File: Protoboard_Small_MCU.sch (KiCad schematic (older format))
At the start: 55 parts, among them J1 POWER, P1 CONN_6, P10 3pin, P11 3pin, P12 3pin, P13 3pin, P14 3pin, P15 3pin, P16 3pin, P17 3pin, P18 2pin, P19 2pin, P2 CONN_6, P20 1pin, P21 2pin, P22 3pin, P23 3pin, P24 3pin, P25 3pin, P26 3pin, P27 3pin, P28 3pin, P29 3pin, P3 1pin, P30 3pin, P31 3pin, P32 3pin, P33 3pin, P34 3pin, P35 3pin, P36 2pin, P37 CONN_7, P38 CONN_7, P39 CONN_7, P4 3pin, P40 CONN_7, P41 V+_RAIL, P42 V-_RAIL, P43 V+_RAIL, P44 V-_RAIL, P45 CONN_8, P46 CONN_8, P47 CONN_8, P48 CONN_8, P49 1pin, P5 3pin, P50 1pin, P51 CONN_6, P52 CONN_6, P6 3pin, P7 3pin, P8 3pin, P9 3pin, SW1 PUSH_SWITCH, U1 DIP28

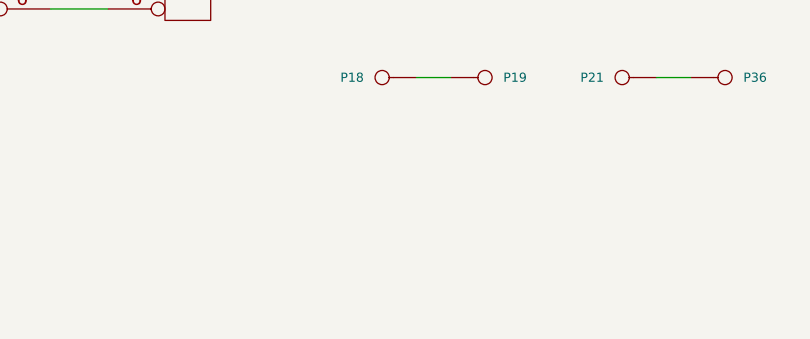
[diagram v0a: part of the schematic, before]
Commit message: Add mounting holes. Greatly increase trace widths. Modify silkscreen to make room for changes.
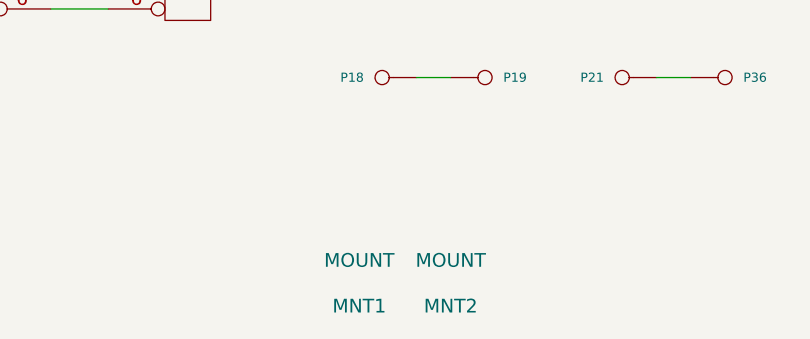
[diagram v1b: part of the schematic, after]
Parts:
- added MNT1, MNT2: MOUNT, symbol MOUNT
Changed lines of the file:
@@
-EESchema Schematic File Version 2  date 1/26/2012 6:15:53 AM
-LIBS:z_audio
-LIBS:z_clock
-LIBS:z_connector
-LIBS:z_digital
-LIBS:z_discrete
-LIBS:z_microcontroller
-LIBS:z_power
-LIBS:z_transducer
-LIBS:z_vintage_ic
+EESchema Schematic File Version 2  date 2/14/2012 2:29:37 AM
+LIBS:zach_components
 LIBS:power
 LIBS:device
@@
 Sheet 1 1
 Title "Protoboard for up to 18pin Microcontrollers (AVR & PIC)"
-Date "26 jan 2012"
+Date "14 feb 2012"
 Rev "1"
 Comp "Zachary Heilig"
@@
 $EndDescr
 $Comp
+L MOUNT MNT2
+U 1 1 4F3A17D5
+P 3800 3650
+F 0 "MNT2" H 3800 3550 60  0000 C CNN
+F 1 "MOUNT" H 3800 3750 60  0000 C CNN
+	1    3800 3650
+	1    0    0    -1
+$EndComp
+$Comp
+L MOUNT MNT1
+U 1 1 4F3A17D3
+P 3400 3650
+F 0 "MNT1" H 3400 3550 60  0000 C CNN
+F 1 "MOUNT" H 3400 3750 60  0000 C CNN
+	1    3400 3650
+	1    0    0    -1
+$EndComp
+$Comp
 L CONN_6 P52

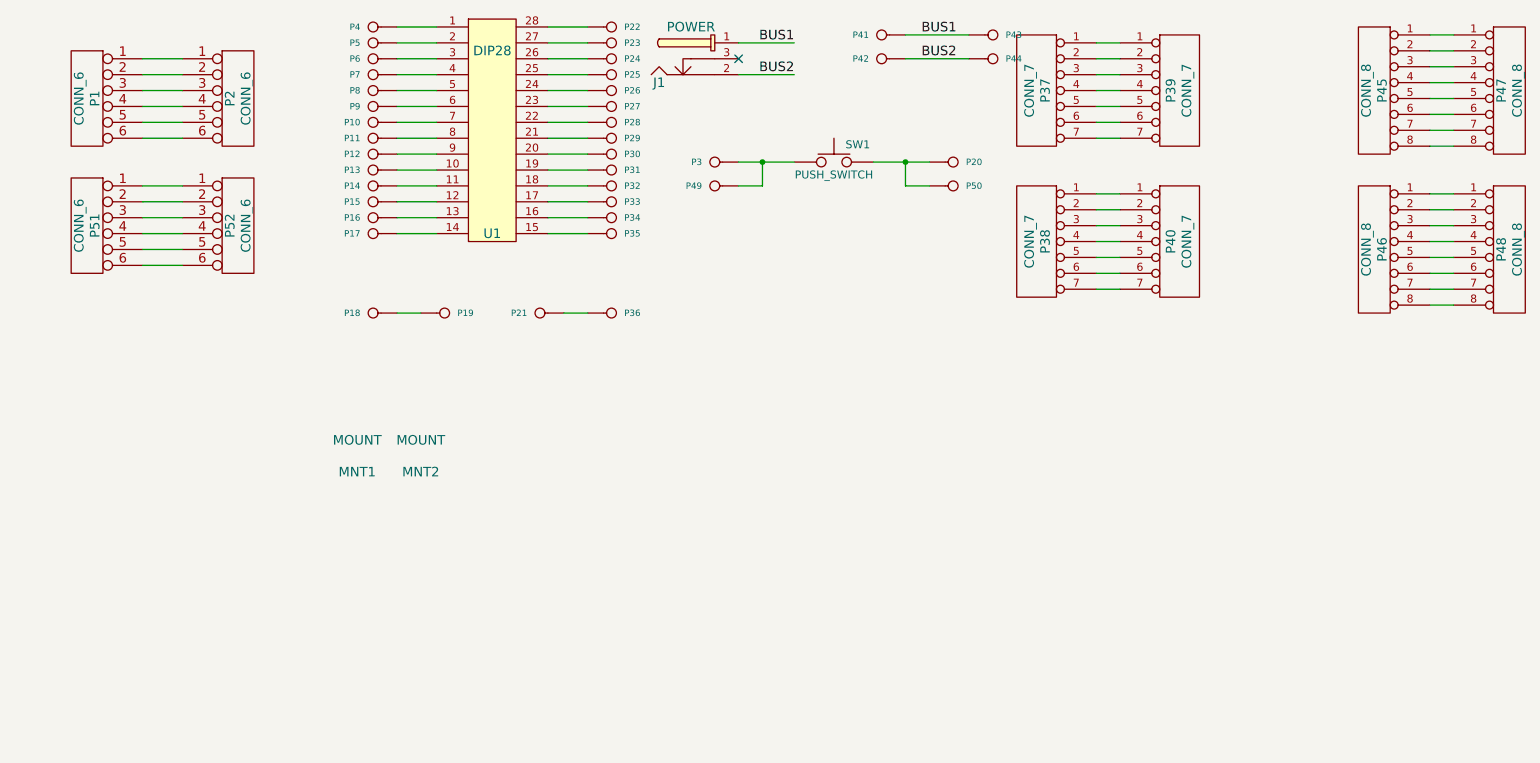
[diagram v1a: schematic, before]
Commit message: Added LDO option to power section.
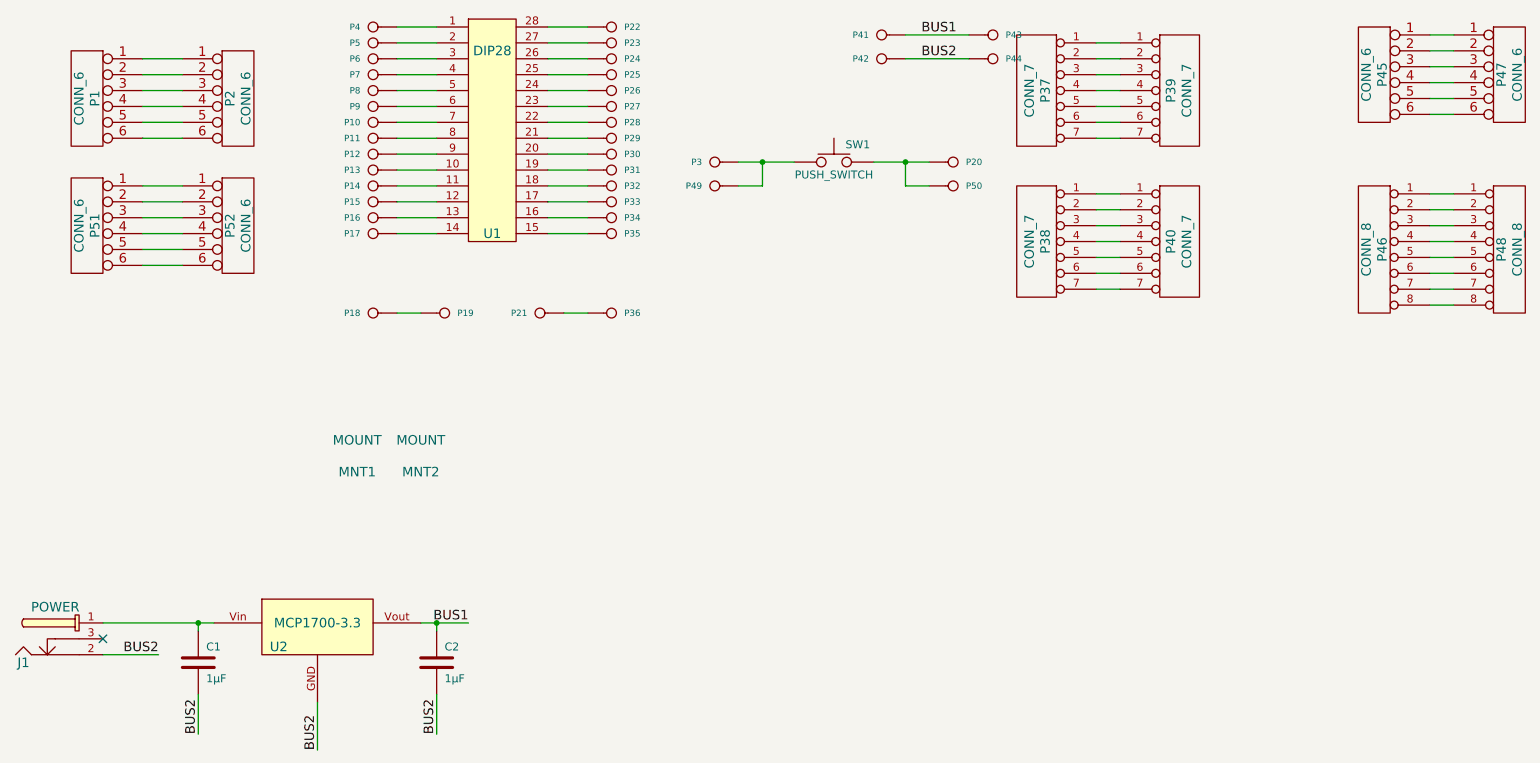
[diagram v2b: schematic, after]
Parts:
- removed P45, P47: CONN_8, symbol CONN_8
- added C1, C2: 1µF, SMD1608-NP, symbol C
- added P45, P47: CONN_6, symbol CONN_6
- added U2: MCP1700-3.3, MCP1700-TO92, symbol MCP1700-3.3
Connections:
- net BUS1: now also C2.1, U2.Vout; no longer J1.1
- net BUS2: now also C1.2, C2.2, U2.GND
- new net: C1.1, J1.1, U2.Vin
- new net: P45.1, P47.1
- new net: P45.2, P47.2
- new net: P45.3, P47.3
- new net: P45.4, P47.4
- new net: P45.5, P47.5
- new net: P45.6, P47.6
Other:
- moved on the sheet: J1
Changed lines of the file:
@@
-EESchema Schematic File Version 2  date 2/14/2012 2:29:37 AM
+EESchema Schematic File Version 2  date 3/18/2012 2:29:13 AM
 LIBS:zach_components
 LIBS:power
@@
 Sheet 1 1
 Title "Protoboard for up to 18pin Microcontrollers (AVR & PIC)"
-Date "14 feb 2012"
+Date "18 mar 2012"
 Rev "1"
 Comp "Zachary Heilig"
@@
 $EndDescr
 $Comp
+L CONN_6 P47
+U 1 1 4F6584D9
+P 10650 1250
+F 0 "P47" V 10600 1250 60  0000 C CNN
+F 1 "CONN_6" V 10700 1250 60  0000 C CNN
+	1    10650 1250
+	1    0    0    -1
+$EndComp
+$Comp
+L CONN_6 P45
+U 1 1 4F6584CB
+P 9800 1250
+F 0 "P45" V 9750 1250 60  0000 C CNN
+F 1 "CONN_6" V 9850 1250 60  0000 C CNN
+	1    9800 1250
+	-1   0    0    -1
+$EndComp
+Wire Wire Line
+	3900 5150 3900 5400
+Connection ~ 2400 4700
+Wire Wire Line
+	2400 4750 2400 4700
+Wire Wire Line
+	3150 5200 3150 5500
+Wire Wire Line
+	2500 4700 1800 4700
+Connection ~ 6850 1800
+Wire Wire Line
+	6850 1800 6850 1950
+Wire Wire Line
+	6850 1950 7000 1950
+Wire Wire Line
+	1800 4900 2150 4900
+Wire Wire Line
+	10150 2700 10300 2700
+Wire Wire Line
+	10150 2600 10300 2600
+Wire Wire Line
+	10150 2400 10300 2400
+Wire Wire Line
+	10150 2200 10300 2200
+Wire Wire Line
+	10150 2000 10300 2000
+Wire Wire Line
+	10150 2100 10300 2100
+Wire Wire Line
+	10150 2300 10300 2300
+Wire Wire Line
+	10150 2500 10300 2500
+Wire Wire Line
+	10150 1500 10300 1500
+Wire Wire Line
+	10150 1300 10300 1300
+Wire Wire Line
+	10150 1100 10300 1100
+Wire Wire Line
+	10150 1000 10300 1000
+Wire Wire Line
+	10150 1200 10300 1200
+Wire Wire Line
+	10150 1400 10300 1400
+Wire Wire Line
+	8050 2500 8200 2500
+Wire Wire Line
+	8050 2300 8200 2300
+Wire Wire Line
+	8050 2100 8200 2100
+Wire Wire Line
+	8050 2000 8200 2000
+Wire Wire Line
+	8050 2200 8200 2200
+Wire Wire Line
+	8050 2400 8200 2400
+Wire Wire Line
+	8050 2600 8200 2600
+Wire Wire Line
+	8050 1650 8200 1650
+Wire Wire Line
+	8050 1450 8200 1450
+Wire Wire Line
+	8050 1250 8200 1250
+Wire Wire Line
+	8050 1050 8200 1050
+Wire Wire Line
+	7250 1000 6850 1000
+Wire Wire Line
+	3650 2750 3800 2750
+Wire Wire Line
+	3650 2250 3900 2250
+Wire Wire Line
+	3650 2050 3900 2050
+Wire Wire Line
+	3650 1950 3900 1950
+Wire Wire Line
+	3650 2150 3900 2150
+Wire Wire Line
+	4600 2150 4850 2150
+Wire Wire Line
+	4600 1950 4850 1950
+Wire Wire Line
+	4600 2050 4850 2050
+Wire Wire Line
+	4600 2250 4850 2250
+Wire Wire Line
+	2050 1650 2300 1650
+Wire Wire Line
+	2050 1450 2300 1450
+Wire Wire Line
+	2050 1250 2300 1250
+Wire Wire Line
+	2050 1150 2300 1150
+Wire Wire Line
+	2050 1350 2300 1350
+Wire Wire Line
+	2050 1550 2300 1550
+Wire Wire Line
+	3650 1750 3900 1750
+Wire Wire Line
+	3650 1550 3900 1550
+Wire Wire Line
+	3650 1350 3900 1350
+Wire Wire Line
+	3650 1150 3900 1150
+Wire Wire Line
+	3650 950  3900 950
+Wire Wire Line
+	3650 1050 3900 1050
+Wire Wire Line
+	3650 1250 3900 1250
+Wire Wire Line
+	3650 1450 3900 1450
+Wire Wire Line
+	3650 1650 3900 1650
+Wire Wire Line
+	3650 1850 3900 1850
+Wire Wire Line
+	4600 1850 4850 1850
+Wire Wire Line
+	4600 1650 4850 1650
+Wire Wire Line
+	4600 1450 4850 1450
+Wire Wire Line
+	4600 1250 4850 1250
+Wire Wire Line
+	4600 1050 4850 1050
+Wire Wire Line
+	4600 950  4850 950
+Wire Wire Line
+	4600 1150 4850 1150
+Wire Wire Line
+	4600 1350 4850 1350
+Wire Wire Line
+	4600 1550 4850 1550
+Wire Wire Line
+	4600 1750 4850 1750
+Wire Wire Line
+	6150 1800 5800 1800
+Wire Wire Line
+	7000 1800 6650 1800
+Wire Wire Line
+	4700 2750 4850 2750
+Wire Wire Line
+	6850 1150 7250 1150
+Wire Wire Line
+	8050 1150 8200 1150
+Wire Wire Line
+	8050 1350 8200 1350
+Wire Wire Line
+	8050 1550 8200 1550
+Wire Wire Line
+	5800 1950 5950 1950
+Wire Wire Line
+	5950 1950 5950 1800
+Connection ~ 5950 1800
+Wire Wire Line
+	2050 2350 2300 2350
+Wire Wire Line
+	2050 2150 2300 2150
+Wire Wire Line
+	2050 1950 2300 1950
+Wire Wire Line
+	2050 2050 2300 2050
+Wire Wire Line
+	2050 2250 2300 2250
+Wire Wire Line
+	2050 2450 2300 2450
+Wire Wire Line
+	3800 4700 4100 4700
+Wire Wire Line
+	3900 4750 3900 4700
+Connection ~ 3900 4700
+Wire Wire Line
+	2400 5150 2400 5400
+Text Label 3900 5400 1    60   ~ 0
+BUS2
+Text Label 2400 5400 1    60   ~ 0
+BUS2
+$Comp
+L C C1
+U 1 1 4F65842D
+P 2400 4950
+F 0 "C1" H 2450 5050 50  0000 L CNN
+F 1 "1µF" H 2450 4850 50  0000 L CNN
+F 2 "SMD1608-NP" H 2400 4950 60  0001 C CNN
+	1    2400 4950
+	1    0    0    -1
+$EndComp
+$Comp
+L C C2
+U 1 1 4F658426
+P 3900 4950
+F 0 "C2" H 3950 5050 50  0000 L CNN
+F 1 "1µF" H 3950 4850 50  0000 L CNN
+F 2 "SMD1608-NP" H 3900 4950 60  0001 C CNN
+	1    3900 4950
+	1    0    0    -1
+$EndComp
+Text Label 3150 5500 1    60   ~ 0
+BUS2
+$Comp
+L MCP1700-3.3 U2
+U 1 1 4F658410
+P 3150 4700
+F 0 "U2" H 2850 4550 60  0000 L CNN
+F 1 "MCP1700-3.3" H 3150 4700 60  0000 C CNN
+F 2 "MCP1700-TO92" H 3150 4800 60  0001 C CNN
+	1    3150 4700
+	1    0    0    -1
+$EndComp
+$Comp
 L MOUNT MNT2
 U 1 1 4F3A17D5
@@
 	-1   0    0    -1
 $EndComp
-Wire Wire Line
-	2050 2450 2300 2450
-Wire Wire Line
-	2050 2250 2300 2250
-Wire Wire Line
-	2050 2050 2300 2050
-Wire Wire Line
-	2050 1950 2300 1950
-Wire Wire Line
-	2050 2150 2300 2150
-Wire Wire Line
-	2050 2350 2300 2350
-Connection ~ 5950 1800
-Wire Wire Line
-	5950 1800 5950 1950
-Wire Wire Line
-	5950 1950 5800 1950
-Wire Wire Line
-	5800 1050 6150 1050
-Wire Wire Line
-	10300 1700 10150 1700
-Wire Wire Line
-	8050 1550 8200 1550
-Wire Wire Line
-	8050 1350 8200 1350
-Wire Wire Line
-	8050 1150 8200 1150
-Wire Wire Line
-	6850 1150 7250 1150
-Wire Wire Line
-	4700 2750 4850 2750
-Wire Wire Line
-	6650 1800 7000 1800
-Wire Wire Line
-	5800 1800 6150 1800
-Wire Wire Line
-	4600 1750 4850 1750
-Wire Wire Line
-	4600 1550 4850 1550
-Wire Wire Line
-	4600 1350 4850 1350
-Wire Wire Line
-	4600 1150 4850 1150
-Wire Wire Line
-	4600 950  4850 950
-Wire Wire Line
-	4600 1050 4850 1050
-Wire Wire Line
-	4600 1250 4850 1250
-Wire Wire Line
-	4600 1450 4850 1450
-Wire Wire Line
-	4600 1650 4850 1650
-Wire Wire Line
-	4600 1850 4850 1850
-Wire Wire Line
-	3650 1850 3900 1850
-Wire Wire Line
-	3650 1650 3900 1650
-Wire Wire Line
-	3650 1450 3900 1450
-Wire Wire Line
-	3650 1250 3900 1250
-Wire Wire Line
-	3650 1050 3900 1050
-Wire Wire Line
-	3650 950  3900 950
-Wire Wire Line
-	3650 1150 3900 1150
-Wire Wire Line
-	3650 1350 3900 1350
-Wire Wire Line
-	3650 1550 3900 1550
-Wire Wire Line
-	3650 1750 3900 1750
-Wire Wire Line
-	2050 1550 2300 1550
-Wire Wire Line
-	2050 1350 2300 1350
-Wire Wire Line
-	2050 1150 2300 1150
-Wire Wire Line
-	2050 1250 2300 1250
-Wire Wire Line
-	2050 1450 2300 1450
-Wire Wire Line
-	2050 1650 2300 1650
-Wire Wire Line
-	4600 2250 4850 2250
-Wire Wire Line
-	4600 2050 4850 2050
-Wire Wire Line
-	4600 1950 4850 1950
-Wire Wire Line
-	4600 2150 4850 2150
-Wire Wire Line
-	3650 2150 3900 2150
-Wire Wire Line
-	3650 1950 3900 1950
-Wire Wire Line
-	3650 2050 3900 2050
-Wire Wire Line
-	3650 2250 3900 2250
-Wire Wire Line
-	3650 2750 3800 2750
-Wire Wire Line
-	7250 1000 6850 1000
-Wire Wire Line
-	8050 1050 8200 1050
-Wire Wire Line
-	8050 1250 8200 1250
-Wire Wire Line
-	8050 1450 8200 1450
-Wire Wire Line
-	8050 1650 8200 1650
-Wire Wire Line
-	8050 2600 8200 2600
-Wire Wire Line
-	8050 2400 8200 2400
-Wire Wire Line
-	8050 2200 8200 2200
-Wire Wire Line
-	8050 2000 8200 2000
-Wire Wire Line
-	8050 2100 8200 2100
-Wire Wire Line
-	8050 2300 8200 2300
-Wire Wire Line
-	8050 2500 8200 2500
-Wire Wire Line
-	10150 1600 10300 1600
-Wire Wire Line
-	10150 1400 10300 1400
-Wire Wire Line
-	10150 1200 10300 1200
-Wire Wire Line
-	10150 1000 10300 1000
-Wire Wire Line
-	10150 1100 10300 1100
-Wire Wire Line
-	10150 1300 10300 1300
-Wire Wire Line
-	10150 1500 10300 1500
-Wire Wire Line
-	10150 2500 10300 2500
-Wire Wire Line
-	10150 2300 10300 2300
-Wire Wire Line
-	10150 2100 10300 2100
-Wire Wire Line
-	10150 2000 10300 2000
-Wire Wire Line
-	10150 2200 10300 2200
-Wire Wire Line
-	10150 2400 10300 2400
-Wire Wire Line
-	10150 2600 10300 2600
-Wire Wire Line
-	10150 2700 10300 2700
-Wire Wire Line
-	5800 1250 6150 1250
-Wire Wire Line
-	7000 1950 6850 1950
-Wire Wire Line
-	6850 1950 6850 1800
-Connection ~ 6850 1800
 $Comp
 L CONN_1 P49
@@
 	1    0    0    -1
 $EndComp
-NoConn ~ 5800 1150
-Text Label 6150 1250 2    60   ~ 0
+NoConn ~ 1800 4800
+Text Label 2150 4900 2    60   ~ 0
 BUS2
-Text Label 6150 1050 2    60   ~ 0
+Text Label 4100 4700 2    60   ~ 0
 BUS1
 $Comp
 L JACK_POWER J1
 U 1 1 4F20BB74
-P 5550 1150
-F 0 "J1" H 5300 1300 60  0000 C CNN
-F 1 "POWER" H 5500 950 60  0000 C CNN
-	1    5550 1150
+P 1550 4800
+F 0 "J1" H 1300 4950 60  0000 C CNN
+F 1 "POWER" H 1500 4600 60  0000 C CNN
+	1    1550 4800
 	1    0    0    1
 $EndComp
@@
 $EndComp
 $Comp
-L CONN_8 P47
-U 1 1 4F1FD0F6
-P 10650 1350
-F 0 "P47" V 10600 1350 60  0000 C CNN
-F 1 "CONN_8" V 10700 1350 60  0000 C CNN
-	1    10650 1350
-	1    0    0    -1
-$EndComp
-$Comp
-L CONN_8 P45
-U 1 1 4F1FD0F5
-P 9800 1350
-F 0 "P45" V 9750 1350 60  0000 C CNN
-F 1 "CONN_8" V 9850 1350 60  0000 C CNN
-	1    9800 1350
-	-1   0    0    -1
-$EndComp
-$Comp
